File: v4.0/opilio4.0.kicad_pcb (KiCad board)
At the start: 4 copper layers, 80 x 40 mm, 83 parts, among them J1 Screw_Terminal_01x02, J2 Conn_01x02_Male, J3 USB_B_Micro, J5 Conn_01x02_Male, Q1 PMV25ENEAR, Q2 PMV25ENEAR, U1 AMS1117-3.3, U5 STM32F103C8T6, Y1 YSX531SL 8MHz, Y2 YST310S 32.768KHz

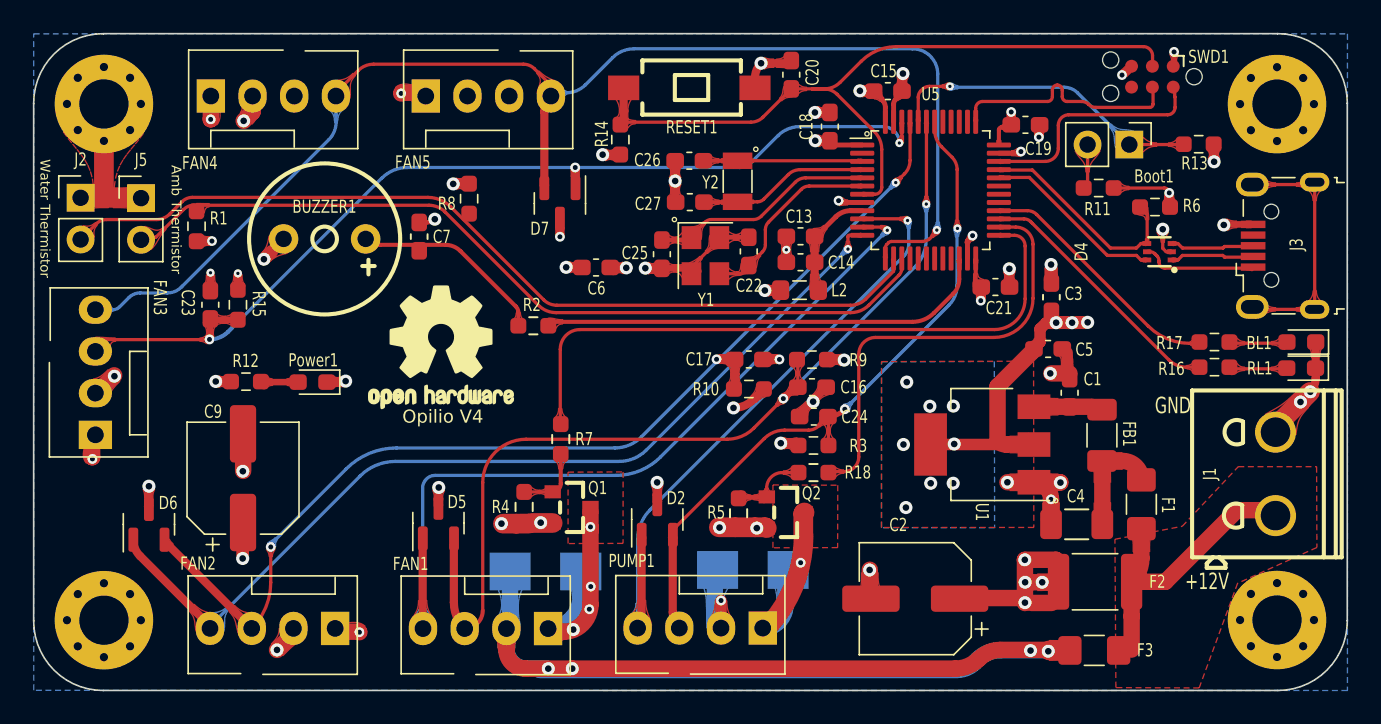
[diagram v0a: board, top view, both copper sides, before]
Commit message: initial board without mosfets
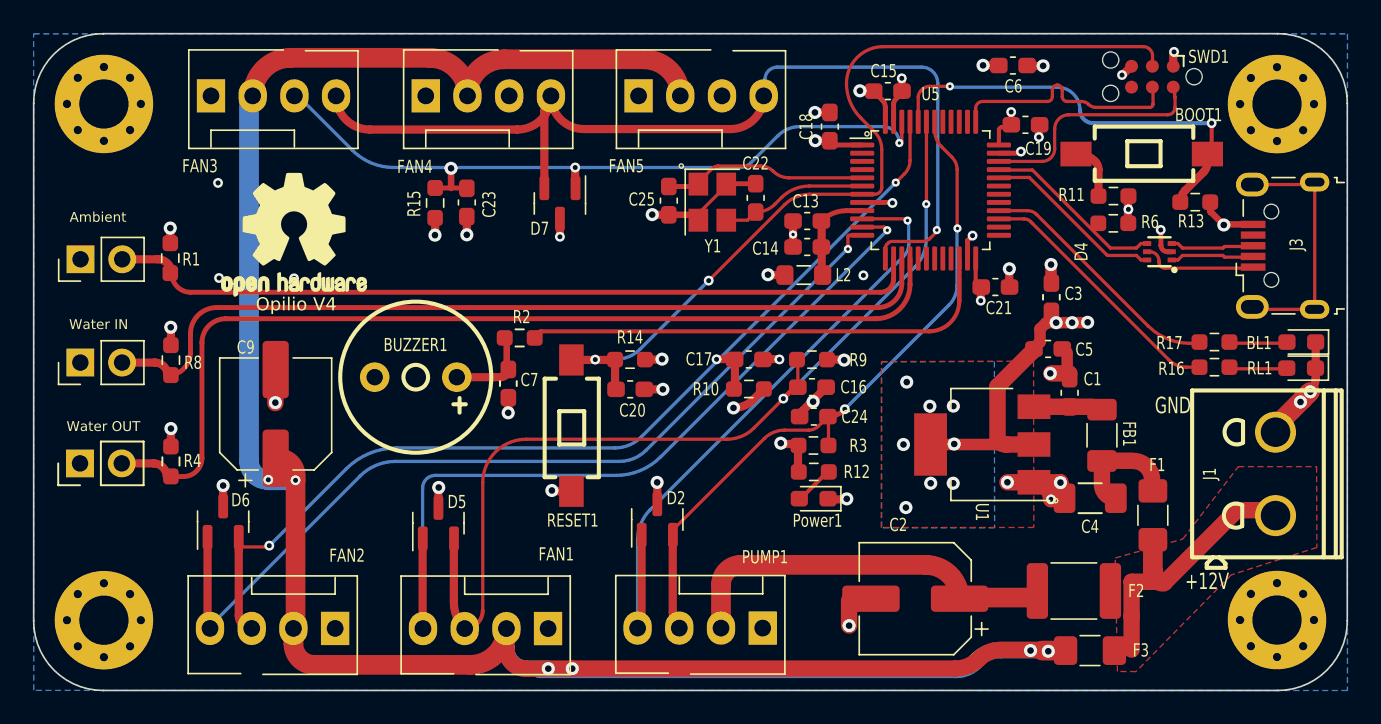
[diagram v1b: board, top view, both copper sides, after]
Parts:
- removed Boot1: Conn_01x02_Male, Connector_PinHeader_2.54mm:PinHeader_1x02_P2.54mm_Vertical
- removed C26, C27: 18pF, Capacitor_SMD:C_0603_1608Metric_Pad1.08x0.95mm_HandSolder
- removed D1, D3: B230, Diode_SMD:D_SMB
- removed Q1, Q2: PMV25ENEAR, easyeda2kicad:SOT-23_L2.9-W1.3-P1.90-LS2.4-BR
- removed R18, R7: 0R, Resistor_SMD:R_0603_1608Metric_Pad0.98x0.95mm_HandSolder
- removed R5: 10K, Resistor_SMD:R_0603_1608Metric_Pad0.98x0.95mm_HandSolder
- removed Y2: YST310S 32.768KHz, Crystal:Crystal_SMD_3215-2Pin_3.2x1.5mm
- added BOOT1: Boot, easyeda2kicad:SW-SMD_L6.0-W3.3-LS8.0, F.Cu at (167.5, 107.3)
- added J4: Conn_01x02_Male, Connector_PinHeader_2.54mm:PinHeader_1x02_P2.54mm_Vertical, F.Cu at (102.8, 126.2)
- R4: value 10K -> 10k
- RESET1: footprint easyedakicad:SW-SMD_L6.0-W3.3-LS8.0 -> easyeda2kicad:SW-SMD_L6.0-W3.3-LS8.0
- moved R12 35.0 mm to (147.5, 126.7)
- moved Power1 31.3 mm to (147.5, 128.3)
- moved C6 28.2 mm to (159.6, 101.9)
- moved FAN3 22.1 mm to (110.8, 103.6), turned to 0 degrees
- moved RESET1 21.8 mm to (132.8, 123.9), turned to 90 degrees
- moved R4 21.7 mm to (108.4, 126.0)
- moved C20 21.5 mm to (136.3, 121.7), turned to 0 degrees
- moved R8 20.6 mm to (108.4, 119.9)
- moved C23 16.8 mm to (126.4, 110.3), turned to 90 degrees
- moved R15 13.5 mm to (124.5, 110.3), turned to 90 degrees
- moved R14 13.4 mm to (136.3, 119.8), turned to 180 degrees
- moved FAN4 13.1 mm to (123.9, 103.6)
- moved FAN5 13.0 mm to (136.8, 103.6)
- moved LOGO1 11.3 mm to (115.9, 112.2)
- moved C7 10.5 mm to (128.9, 121.3), turned to -90 degrees
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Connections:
- FAN1 pad 1: F_GND -> GND
- FAN2 pad 1: F_GND -> GND
- FAN3 pad 1: F_GND -> GND
- FAN4 pad 1: F_GND -> GND
- FAN5 pad 1: F_GND -> GND
- J2 pad 2: THERM_READ_W -> WATER_IN_T
- J5 pad 2: THERM_READ_A -> AMBIENT_T
- PUMP1 pad 1: P_GND -> GND
- R1 pad 1: THERM_READ_A -> AMBIENT_T
- R4 pad 1: GND -> WATER_OUT_T
- R4 pad 2: Net-(Q1-Pad1) -> +3.3V
- R8 pad 1: THERM_READ_W -> WATER_IN_T
- U5 pad 14: THERM_READ_W -> AMBIENT_T
- U5 pad 15: THERM_READ_A -> WATER_IN_T
- U5 pad 16: unconnected-(U5-Pad16) -> WATER_OUT_T
- U5 pad 3: CIN -> unconnected-(U5-Pad3)
- U5 pad 4: COUT -> unconnected-(U5-Pad4)
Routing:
- net +12VF(F): track 81.9 -> 155.7 mm, vias 8 -> 6
- net WATER_OUT_T: track 0.00 -> 59.5 mm
- net THERM_READ_W: track 54.6 -> 0.00 mm
- net WATER_IN_T: track 0.00 -> 52.9 mm
- net THERM_READ_A: track 50.7 -> 0.00 mm
- net AMBIENT_T: track 0.00 -> 49.7 mm
- net FAN_EN: track 39.6 -> 0.00 mm
- net PUMP_EN: track 26.9 -> 0.00 mm
- net GND: track 76.5 -> 55.5 mm, vias 39 -> 38
- net F_GND: track 19.4 -> 0.00 mm, vias 8 -> 0
- net PWM_OUT4: track 80.8 -> 61.8 mm
- net PWM_READ4: track 59.3 -> 44.6 mm
- net P_GND: track 11.2 -> 0.00 mm, vias 1 -> 0
- net COUT: track 10.4 -> 0.00 mm
- net CIN: track 9.62 -> 0.00 mm
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- removed copper zone on In2.Cu, net +12VF(F)
- removed copper zone on In2.Cu, net +12VF(P)
- removed copper zone on F.Cu, net F_GND
- removed copper zone on In1.Cu, net F_GND
- removed copper zone on F.Cu, net P_GND
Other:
- board text added: "Ambient"
- board text added: "Water IN"
- board text added: "Water OUT"
- board text removed: "Amb Thermistor"
- board text removed: "Water Thermistor"

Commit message: cleanup and reroute
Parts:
- removed C24: 10nF, Capacitor_SMD:C_0603_1608Metric_Pad1.08x0.95mm_HandSolder
- removed C25: 30pF, Capacitor_SMD:C_0603_1608Metric_Pad1.08x0.95mm_HandSolder
- removed FAN1: Fan_4pin, Custom:FanPinHeader_1x04_P2.54mm_Vertical_no_hole
- removed U5: STM32F103C8T6, Package_QFP:LQFP-48_7x7mm_P0.5mm
- added C10: 100nF, Capacitor_SMD:C_0603_1608Metric_Pad1.08x0.95mm_HandSolder, F.Cu at (152.1, 103.5)
- added C11: 100nF, Capacitor_SMD:C_0603_1608Metric_Pad1.08x0.95mm_HandSolder, F.Cu at (160.3, 105.5)
- added C12: 1uF, Capacitor_SMD:C_0603_1608Metric_Pad1.08x0.95mm_HandSolder, F.Cu at (147.1, 113.0)
- added C8: 100nF, Capacitor_SMD:C_0603_1608Metric_Pad1.08x0.95mm_HandSolder, F.Cu at (158.4, 115.5)
- added D1: USBLC6-2SC6, easyeda2kicad:SOT-666-6_L1.6-W1.2-P0.50-LS1.6-BL, F.Cu at (168.6, 113.3)
- added D3: SP0502BAHT, Package_TO_SOT_SMD:SOT-23, F.Cu at (138.0, 129.6)
- added FAN6: Fan_4pin, Custom:FanPinHeader_1x04_P2.54mm_Vertical_no_hole, F.Cu at (136.8, 103.8)
- added L1: 4.7uH, Inductor_SMD:L_Bourns-SRN4018, F.Cu at (160.4, 121.5)
- added R18: 1k, Resistor_SMD:R_0603_1608Metric_Pad0.98x0.95mm_HandSolder, F.Cu at (143.6, 121.4)
- added R5: 165R, Resistor_SMD:R_0603_1608Metric_Pad0.98x0.95mm_HandSolder, F.Cu at (172.1, 120.4)
- added R7: 1.65K, Resistor_SMD:R_0603_1608Metric_Pad0.98x0.95mm_HandSolder, F.Cu at (147.4, 126.7)
- added TP1: 3v3, TestPoint:TestPoint_Pad_D1.0mm, F.Cu at (156.1, 120.7)
- added U2: STM32F103C8T6, Package_QFP:LQFP-48_7x7mm_P0.5mm, F.Cu at (154.6, 109.5)
- added Y2: YST310S 32.768KHz, Crystal:Crystal_SMD_3215-2Pin_3.2x1.5mm, F.Cu at (141.0, 109.4)
- C1: value 10uF -> 30pF
- C13: value 10nF -> 10uF
- C14: value 1uF -> 10uF
- C15, C18: value 100nF -> 220uF; footprint Capacitor_SMD:C_0603_1608Metric_Pad1.08x0.95mm_HandSolder -> Capacitor_SMD:CP_Elec_6.3x7.7
- C19, C21: value 100nF -> 10nF
- C2: value 220uF -> 30pF; footprint Capacitor_SMD:CP_Elec_6.3x7.7 -> Capacitor_SMD:C_0603_1608Metric_Pad1.08x0.95mm_HandSolder
- C22: value 30pF -> 18pF
- C23: value 10nF -> 18pF
- C3: value 10uF -> 100nF
- C4: value 22uF -> 10uF; footprint Capacitor_SMD:C_1206_3216Metric_Pad1.33x1.80mm_HandSolder -> Capacitor_SMD:C_0603_1608Metric_Pad1.08x0.95mm_HandSolder
- C5, C6: value 10uF -> 10nF
- C7: value 100nF -> 10uF
- C9: value 220uF -> 100nF; footprint Capacitor_SMD:CP_Elec_6.3x7.7 -> Capacitor_SMD:C_0603_1608Metric_Pad1.08x0.95mm_HandSolder
- D2, D7: value SP0502BAHT -> B230A; footprint Package_TO_SOT_SMD:SOT-23 -> Diode_SMD:D_SMA
- D4: value USBLC6-2SC6 -> SP0502BAHT; footprint easyeda2kicad:SOT-666-6_L1.6-W1.2-P0.50-LS1.6-BL -> Package_TO_SOT_SMD:SOT-23
- J2: value Conn_01x02_Male -> USB_B_Micro; footprint Connector_PinHeader_2.54mm:PinHeader_1x02_P2.54mm_Vertical -> Custom:USB_Micro-B_Wuerth_629105150521_narrow_holes
- J3: value USB_B_Micro -> Conn_01x02_Male; footprint Custom:USB_Micro-B_Wuerth_629105150521_narrow_holes -> Connector_PinHeader_2.54mm:PinHeader_1x02_P2.54mm_Vertical
- R1: value 10k -> 100k
- R10: value 1k -> 24k
- R11: value 10K -> 10k
- R12: value 1.65K -> 1k
- R13: value 100k -> 1k
- R16: value 165R -> 100R
- R17: value R660 -> 10k
- R2: value 100R -> 10K
- R3: value 1k -> 10k
- R4: value 10k -> 1k5
- R6: value 1k5 -> R660
- R8: value 10k -> 22R
- R9: value 1k -> 75k
- U1: value AMS1117-3.3 -> EUP3458; footprint Package_TO_SOT_SMD:SOT-223-3_TabPin2 -> Package_TO_SOT_SMD:SOT-23-6_Handsoldering
- moved J2 73.4 mm to (175.9, 112.9)
- moved J3 73.2 mm to (102.9, 113.8)
- moved R17 64.0 mm to (108.3, 126.0), turned to 90 degrees
- moved R1 62.4 mm to (170.6, 110.2), turned to 0 degrees
- moved R4 59.2 mm to (165.7, 111.5), turned to 180 degrees
- moved R11 57.6 mm to (108.3, 113.7), turned to 90 degrees
- moved R8 54.3 mm to (161.9, 128.6), turned to 180 degrees
- moved D4 47.0 mm to (124.6, 129.9)
- moved R13 46.3 mm to (124.4, 110.5), turned to 90 degrees
- moved D7 45.8 mm to (169.9, 136.2)
- moved R16 42.1 mm to (129.8, 118.4), turned to 180 degrees
- moved C9 38.3 mm to (148.7, 105.6)
- moved C18 37.8 mm to (114.8, 122.8)
- moved R2 37.1 mm to (165.7, 109.9)
- moved C7 36.3 mm to (159.6, 101.9), turned to 0 degrees
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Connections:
- BOOT1 pad 2: Net-(R11-Pad2) -> Net-(BOOT1-Pad2)
- C1 pad 1: Net-(C1-Pad1) -> OSCOUT
- C13 pad 1: VDDA -> +3.3V
- C14 pad 1: VDDA -> +3.3V
- C15 pad 1: +3.3V -> +12VF(P)
- C16 pad 2: PWM_READ2 -> PWM_READ1
- C17 pad 2: PWM_READ3 -> PWM_READ4
- C18 pad 1: +3.3V -> +12VF(F)
- C19 pad 1: +3.3V -> GND
- C19 pad 2: GND -> PWM_READ2
- C2 pad 1: +12VF(P) -> GND
- C2 pad 2: GND -> OSCIN
- C20 pad 1: NRST -> Net-(BUZZER1-Pad1)
- C21 pad 1: +3.3V -> GND
- C21 pad 2: GND -> PWM_READ3
- C22 pad 1: OSCOUT -> CIN
- C23 pad 1: GND -> COUT
- C23 pad 2: PWM_READ4 -> GND
- C3 pad 1: +3.3V -> NRST
- C5 pad 1: +3.3V -> Net-(C5-Pad1)
- C5 pad 2: GND -> Net-(C5-Pad2)
- C6 pad 1: +3.3V -> VDDA
- C7 pad 1: Net-(BUZZER1-Pad1) -> +3.3V
- C9 pad 1: +12VF(F) -> +3.3V
- D2 pad 1: PWM_OUT1 -> Net-(C5-Pad1)
- D2 pad 2: PWM_READ1 -> GND
- D4 pad 1: USB_CON_D- -> PWM_OUT2
- D4 pad 2: GND -> PWM_READ2
- D4 pad 3: USB_CON_D+ -> GND
- D5 pad 1: PWM_OUT2 -> PWM_OUT3
- D5 pad 2: PWM_READ2 -> PWM_READ3
- D6 pad 1: PWM_OUT3 -> PWM_READ4
- D6 pad 2: PWM_READ3 -> PWM_OUT4
- D7 pad 1: PWM_READ4 -> +12V
- D7 pad 2: PWM_OUT4 -> GND
- F1 pad 2: Net-(C4-Pad1) -> Net-(F1-Pad2)
- FAN2 pad 3: PWM_READ3 -> PWM_READ2
- FAN2 pad 4: PWM_OUT3 -> PWM_OUT2
- FAN3 pad 3: PWM_READ4 -> PWM_READ3
- FAN3 pad 4: PWM_OUT4 -> PWM_OUT3
- FAN4 pad 3: unconnected-(FAN4-Pad3) -> PWM_READ4
- FB1 pad 1: Net-(C1-Pad1) -> Net-(C4-Pad1)
- FB1 pad 2: Net-(C4-Pad1) -> Net-(F1-Pad2)
- J2 pad 1: GND -> +5V
- J2 pad 2: WATER_IN_T -> USB_CON_D-
- J3 pad 1: +5V -> GND
- J3 pad 2: USB_CON_D- -> AMBIENT_T
- J4 pad 2: WATER_OUT_T -> WATER_IN_T
- J5 pad 2: AMBIENT_T -> WATER_OUT_T
- R1 pad 1: AMBIENT_T -> BOOT0
- R1 pad 2: +3.3V -> GND
- R10 pad 1: +3.3V -> BUCK_FB
- R10 pad 2: PWM_READ3 -> GND
- R11 pad 1: +3.3V -> AMBIENT_T
- R11 pad 2: Net-(R11-Pad2) -> +3.3V
- R12 pad 2: Net-(Power1-Pad2) -> PWM_READ1
- R13 pad 1: BOOT0 -> +3.3V
- R13 pad 2: GND -> PWM_READ4
- R14 pad 1: +3.3V -> WATER_IN_T
- R14 pad 2: NRST -> +3.3V
- R15 pad 2: PWM_READ4 -> PWM_READ2
- R16 pad 1: RED_LED -> BUZZER
- R16 pad 2: Net-(R16-Pad2) -> Net-(BUZZER1-Pad1)
- R17 pad 1: BLUE_LED -> WATER_OUT_T
- R17 pad 2: Net-(BL1-Pad2) -> +3.3V
- R2 pad 1: BUZZER -> +3.3V
- R2 pad 2: Net-(BUZZER1-Pad1) -> Net-(BOOT1-Pad2)
- R3 pad 2: PWM_READ1 -> NRST
- R4 pad 1: WATER_OUT_T -> +3.3V
- R4 pad 2: +3.3V -> USB_D+
- R6 pad 1: +3.3V -> BLUE_LED
- R6 pad 2: USB_D+ -> Net-(BL1-Pad2)
- R8 pad 1: WATER_IN_T -> Net-(C4-Pad1)
- R8 pad 2: +3.3V -> Net-(R8-Pad2)
- R9 pad 2: PWM_READ2 -> BUCK_FB
- RL1 pad 2: Net-(R16-Pad2) -> Net-(R5-Pad2)
- U1 pad 1: GND -> Net-(C5-Pad2)
- U1 pad 2: +3.3V -> GND
- U1 pad 3: Net-(C1-Pad1) -> BUCK_FB
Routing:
- net +12VF(F): track 155.7 -> 183.2 mm, vias 6 -> 10
- net +3.3V: track 44.2 -> 25.4 mm, vias 27 -> 20
- net unconnected-(J3-Pad6): track 14.6 -> 0.00 mm
- net unconnected-(J2-Pad6): track 0.00 -> 14.6 mm
- net CIN: track 0.00 -> 14.0 mm
- net Net-(C5-Pad1): track 0.00 -> 9.70 mm
- net GND: track 55.5 -> 64.6 mm
- net COUT: track 0.00 -> 8.61 mm
- net +12VF(P): track 23.9 -> 31.3 mm
- net Net-(C5-Pad2): track 0.00 -> 7.32 mm
- net OSCIN: track 12.2 -> 16.0 mm
- net BUCK_FB: track 0.00 -> 3.54 mm
- net Net-(C1-Pad1): track 3.50 -> 0.00 mm
- net Net-(R11-Pad2): track 3.44 -> 0.00 mm
- net Net-(BOOT1-Pad2): track 0.00 -> 3.34 mm
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- removed copper zone on B.Cu, net +3.3V
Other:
- board text added: "Liquid IN"
- board text added: "Liquid OUT"
- board text added: "VID 0x1209 PID 0x2442"
- board text added: "https://github.com/mygnu/opilio"
- board text removed: "Water IN"
- board text removed: "Water OUT"
- board text removed: "https://github.com/mygnu/opilio-firmware"
